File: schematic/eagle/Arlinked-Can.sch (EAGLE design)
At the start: 18 parts, among them U1 MCP2515, U2 TJA1050, U3 V_REG_LDOSMD, Y1 xtal

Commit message: Added schematic/protel/arlinked-can-v0.1-print-10p.pcb
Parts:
- added J8: JUMPER-1X3, Arlinked:JUMPER-1X3
- added R3: 10k, SparkFun:RESISTOR0603-RES
- added U$1: PAD, Arlinked:PAD
- C1, C3: value (none) -> 10uF
- C2: value (none) -> 407
- JP1: value (none) -> HOLE1
- JP2: value (none) -> HOLE2
- JP3: value (none) -> INPUT_HEADER
- LED1: value (none) -> 2mA
- R2: value (none) -> 320R
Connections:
- removed net N$7: F1.1, U3.OUT
- new net N$10: J8.J-2, R3.1
- new net S: J8.J-0, U2.S
- new net VCC-DIRECT: F1.1, JP7.J-2, U3.OUT
- net GND: now also J8.J-1; no longer U2.S
- net VCC: now also R3.2; no longer JP7.J-2
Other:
- moved on the sheet: C1, C2, F1, JP1, JP2, LED1, R1, R2, U1, U2, Y1

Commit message: Added Arlinked CanBus module v0.2
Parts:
- added C4, C5: (no value), SparkFun:CAP0402-CAP
- added LED2: 2mA Red, SparkFun:LED0603
- added R4: 320R, SparkFun:RESISTOR0402-RES
- added Y2: (no value), Arlinked:CRYSTALPAD-ONLY
- R1: device SparkFun:RESISTOR1206 -> SparkFun:RESISTOR0603-RES
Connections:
- net N$6 renamed LED1-CAN-2
- net VCC-DIRECT renamed VCC-FUSE
- removed net N$3: U1.OSC2, Y1.1
- removed net N$4: U1.OSC1, Y1.3
- new net LED2-POWER-2: LED2.A, R4.1
- new net OSC1: C4.1, U1.OSC1, Y1.3, Y2.2
- new net OSC2: C5.2, U1.OSC2, Y1.1, Y2.1
- net GND: now also C4.2, C5.1, LED2.C
- net VCC: now also R4.2
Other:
- moved on the sheet: LED1, R2, Y1
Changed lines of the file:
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@@
 <part name="GND4" library="SparkFun" deviceset="GND" device=""/>
 <part name="GND5" library="SparkFun" deviceset="GND" device=""/>
-<part name="R1" library="SparkFun" deviceset="RESISTOR" device="1206" value="10k"/>
+<part name="R1" library="SparkFun" deviceset="RESISTOR" device="0603-RES" value="10k"/>
 <part name="P+4" library="SparkFun" deviceset="VCC" device=""/>
 <part name="U1" library="Arlinked" deviceset="MCP2515" device=""/>
@@
 <part name="R3" library="SparkFun" deviceset="RESISTOR" device="0603-RES" value="10k"/>
 <part name="U$1" library="Arlinked" deviceset="PAD" device=""/>
+<part name="C4" library="SparkFun" deviceset="CAP" device="0402-CAP"/>
+<part name="C5" library="SparkFun" deviceset="CAP" device="0402-CAP"/>
+<part name="GND8" library="SparkFun" deviceset="GND" device=""/>
+<part name="Y2" library="Arlinked" deviceset="CRYSTAL" device="PAD-ONLY"/>
+<part name="LED2" library="SparkFun" deviceset="LED" device="0603" value="2mA Red"/>
+<part name="R4" library="SparkFun" deviceset="RESISTOR" device="0402-RES" value="320R"/>
+<part name="GND9" library="SparkFun" deviceset="GND" device=""/>
+<part name="P+5" library="SparkFun" deviceset="VCC" device=""/>
 </parts>
 <sheets>
@@
 <instance part="C2" gate="G$1" x="50.8" y="45.72"/>
 <instance part="GND1" gate="1" x="43.18" y="40.64"/>
-<instance part="Y1" gate="G$1" x="111.76" y="7.62"/>
-<instance part="GND2" gate="1" x="111.76" y="-2.54"/>
+<instance part="Y1" gate="G$1" x="111.76" y="12.7"/>
+<instance part="GND2" gate="1" x="111.76" y="2.54"/>
 <instance part="GND3" gate="1" x="88.9" y="2.54"/>
 <instance part="P+3" gate="1" x="55.88" y="71.12"/>
@@
 <instance part="C3" gate="G$1" x="-12.7" y="40.64"/>
 <instance part="F1" gate="G$1" x="30.48" y="50.8"/>
-<instance part="P+1" gate="1" x="50.8" y="50.8"/>
-<instance part="LED1" gate="G$1" x="124.46" y="5.08"/>
-<instance part="R2" gate="G$1" x="124.46" y="12.7" rot="R90"/>
-<instance part="GND7" gate="1" x="124.46" y="-2.54"/>
+<instance part="P+1" gate="1" x="43.18" y="50.8"/>
+<instance part="LED1" gate="G$1" x="124.46" y="30.48"/>
+<instance part="R2" gate="G$1" x="124.46" y="38.1" rot="R90"/>
+<instance part="GND7" gate="1" x="124.46" y="22.86"/>
 <instance part="U$2" gate="G$1" x="5.08" y="15.24" rot="MR180"/>
 <instance part="U2" gate="G$1" x="76.2" y="68.58"/>
@@
 <instance part="R3" gate="G$1" x="104.14" y="58.42" rot="R180"/>
 <instance part="U$1" gate="G$1" x="25.4" y="-22.86"/>
+<instance part="C4" gate="G$1" x="129.54" y="5.08"/>
+<instance part="C5" gate="G$1" x="124.46" y="7.62" rot="R180"/>
+<instance part="GND8" gate="1" x="124.46" y="0"/>
+<instance part="Y2" gate="G$1" x="127" y="10.16"/>
+<instance part="LED2" gate="G$1" x="-33.02" y="40.64"/>
+<instance part="R4" gate="G$1" x="-33.02" y="48.26" rot="R90"/>
+<instance part="GND9" gate="1" x="-33.02" y="33.02"/>
+<instance part="P+5" gate="1" x="-33.02" y="53.34"/>
 </instances>
 <busses>
@@
 <junction x="50.8" y="50.8"/>
 <junction x="43.18" y="50.8"/>
+</segment>
+<segment>
+<pinref part="R4" gate="G$1" pin="2"/>
+<pinref part="P+5" gate="1" pin="VCC"/>
 </segment>
 </net>
@@
 <pinref part="GND5" gate="1" pin="GND"/>
 </segment>
+<segment>
+<pinref part="C4" gate="G$1" pin="2"/>
+<pinref part="GND8" gate="1" pin="GND"/>
+<wire x1="129.54" y1="2.54" x2="124.46" y2="2.54" width="0.1524" layer="91"/>
+<pinref part="C5" gate="G$1" pin="1"/>
+<junction x="124.46" y="2.54"/>
+</segment>
+<segment>
+<pinref part="LED2" gate="G$1" pin="C"/>
+<pinref part="GND9" gate="1" pin="GND"/>
+</segment>
 </net>
 <net name="N$1" class="0">
@@
 </segment>
 </net>
-<net name="N$3" class="0">
+<net name="OSC2" class="0">
+<segment>
+<wire x1="119.38" y1="15.24" x2="124.46" y2="15.24" width="0.1524" layer="91"/>
+<wire x1="124.46" y1="15.24" x2="124.46" y2="10.16" width="0.1524" layer="91"/>
+<pinref part="C5" gate="G$1" pin="2"/>
+<pinref part="Y2" gate="G$1" pin="1"/>
+<label x="119.38" y="15.24" size="1.778" layer="95"/>
+<junction x="124.46" y="10.16"/>
+</segment>
 <segment>
 <pinref part="Y1" gate="G$1" pin="1"/>
+<wire x1="109.22" y1="15.24" x2="109.22" y2="12.7" width="0.1524" layer="91"/>
 <wire x1="106.68" y1="15.24" x2="109.22" y2="15.24" width="0.1524" layer="91"/>
-<wire x1="109.22" y1="15.24" x2="109.22" y2="7.62" width="0.1524" layer="91"/>
 <pinref part="U1" gate="G$1" pin="OSC2"/>
-</segment>
-</net>
-<net name="N$4" class="0">
+<junction x="109.22" y="12.7"/>
+</segment>
+</net>
+<net name="OSC1" class="0">
+<segment>
+<wire x1="119.38" y1="17.78" x2="129.54" y2="17.78" width="0.1524" layer="91"/>
+<wire x1="129.54" y1="17.78" x2="129.54" y2="10.16" width="0.1524" layer="91"/>
+<pinref part="C4" gate="G$1" pin="1"/>
+<pinref part="Y2" gate="G$1" pin="2"/>
+<label x="119.38" y="17.78" size="1.778" layer="95"/>
+<junction x="129.54" y="10.16"/>
+</segment>
 <segment>
 <pinref part="Y1" gate="G$1" pin="3"/>
+<wire x1="114.3" y1="17.78" x2="114.3" y2="12.7" width="0.1524" layer="91"/>
 <wire x1="106.68" y1="17.78" x2="114.3" y2="17.78" width="0.1524" layer="91"/>
-<wire x1="114.3" y1="17.78" x2="114.3" y2="7.62" width="0.1524" layer="91"/>
 <pinref part="U1" gate="G$1" pin="OSC1"/>
+<junction x="114.3" y="12.7"/>
 </segment>
 </net>
@@
 <segment>
 <pinref part="U1" gate="G$1" pin="SCK"/>
-<wire x1="106.68" y1="27.94" x2="124.46" y2="27.94" width="0.1524" layer="91"/>
+<wire x1="106.68" y1="27.94" x2="119.38" y2="27.94" width="0.1524" layer="91"/>
 <label x="109.22" y="27.94" size="1.778" layer="95"/>
-<pinref part="R2" gate="G$1" pin="2"/>
-<wire x1="124.46" y1="27.94" x2="124.46" y2="17.78" width="0.1524" layer="91"/>
 </segment>
 <segment>
@@
 <wire x1="55.88" y1="7.62" x2="45.72" y2="7.62" width="0.1524" layer="91"/>
 <label x="45.72" y="7.62" size="1.778" layer="95"/>
+</segment>
+<segment>
+<pinref part="R2" gate="G$1" pin="2"/>
+<wire x1="124.46" y1="43.18" x2="121.92" y2="43.18" width="0.1524" layer="91"/>
+<label x="119.38" y="43.18" size="1.778" layer="95"/>
 </segment>
 </net>
@@
 </segment>
 </net>
-<net name="N$6" class="0">
+<net name="LED1-CAN-2" class="0">
 <segment>
 <pinref part="R2" gate="G$1" pin="1"/>
@@
 </segment>
 </net>
-<net name="VCC-DIRECT" class="0">
+<net name="VCC-FUSE" class="0">
 <segment>
 <pinref part="U3" gate="G$1" pin="OUT"/>
@@
 <wire x1="20.32" y1="50.8" x2="20.32" y2="55.88" width="0.1524" layer="91"/>
 <label x="17.78" y="55.88" size="1.778" layer="95"/>
+<junction x="20.32" y="50.8"/>
 </segment>
 <segment>
@@
 </segment>
 </net>
+<net name="LED2-POWER-2" class="0">
+<segment>
+<pinref part="R4" gate="G$1" pin="1"/>
+<pinref part="LED2" gate="G$1" pin="A"/>
+</segment>
+</net>

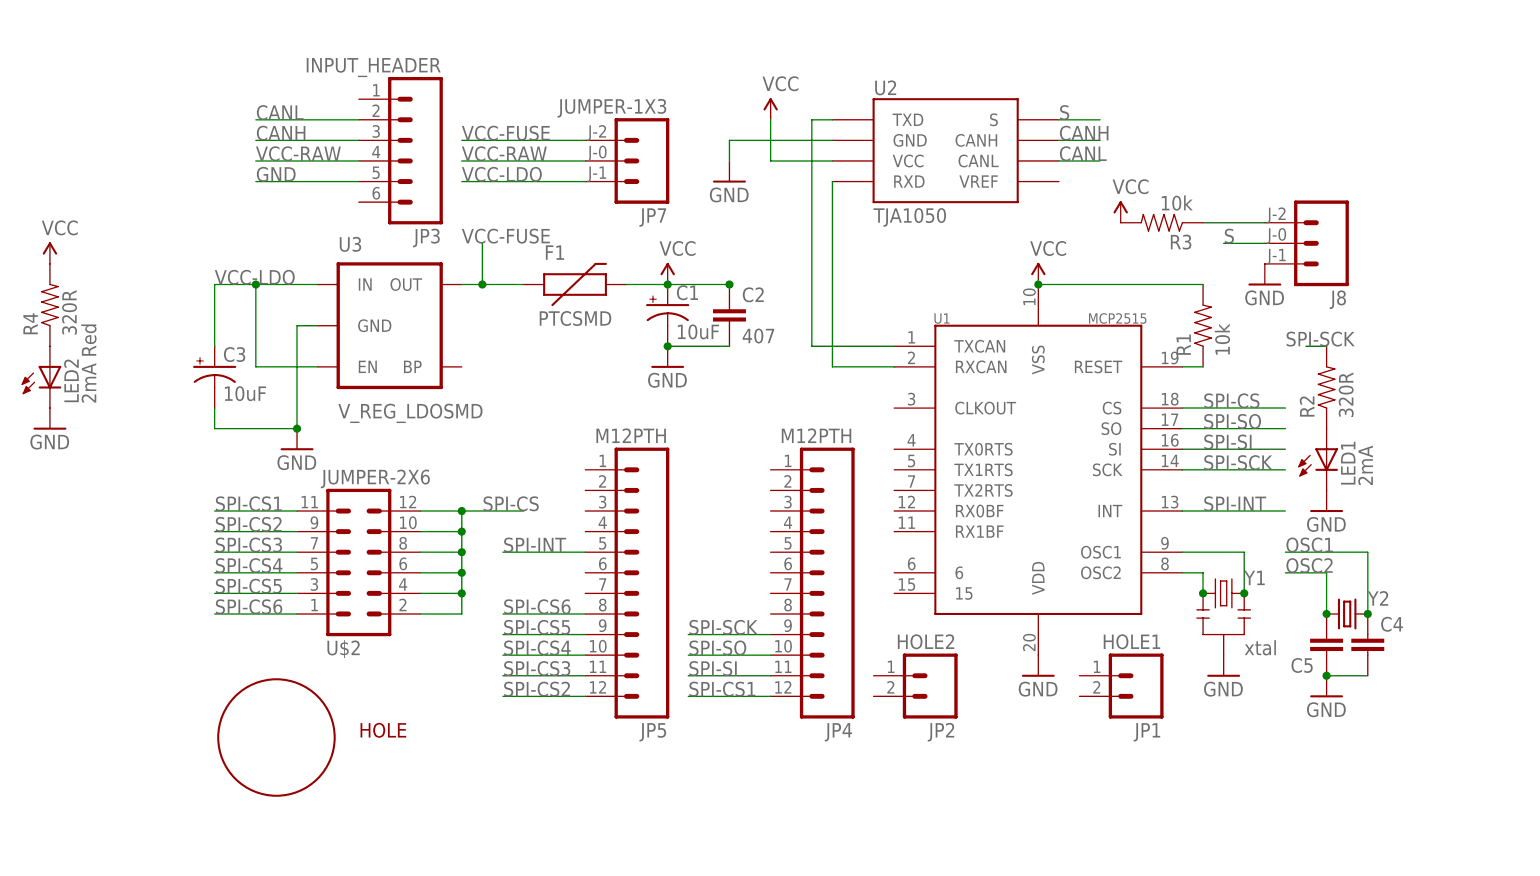
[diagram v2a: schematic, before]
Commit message: CanBus module v0.2 schematic and PCB release  #4 fixed Vdd Vss mistake
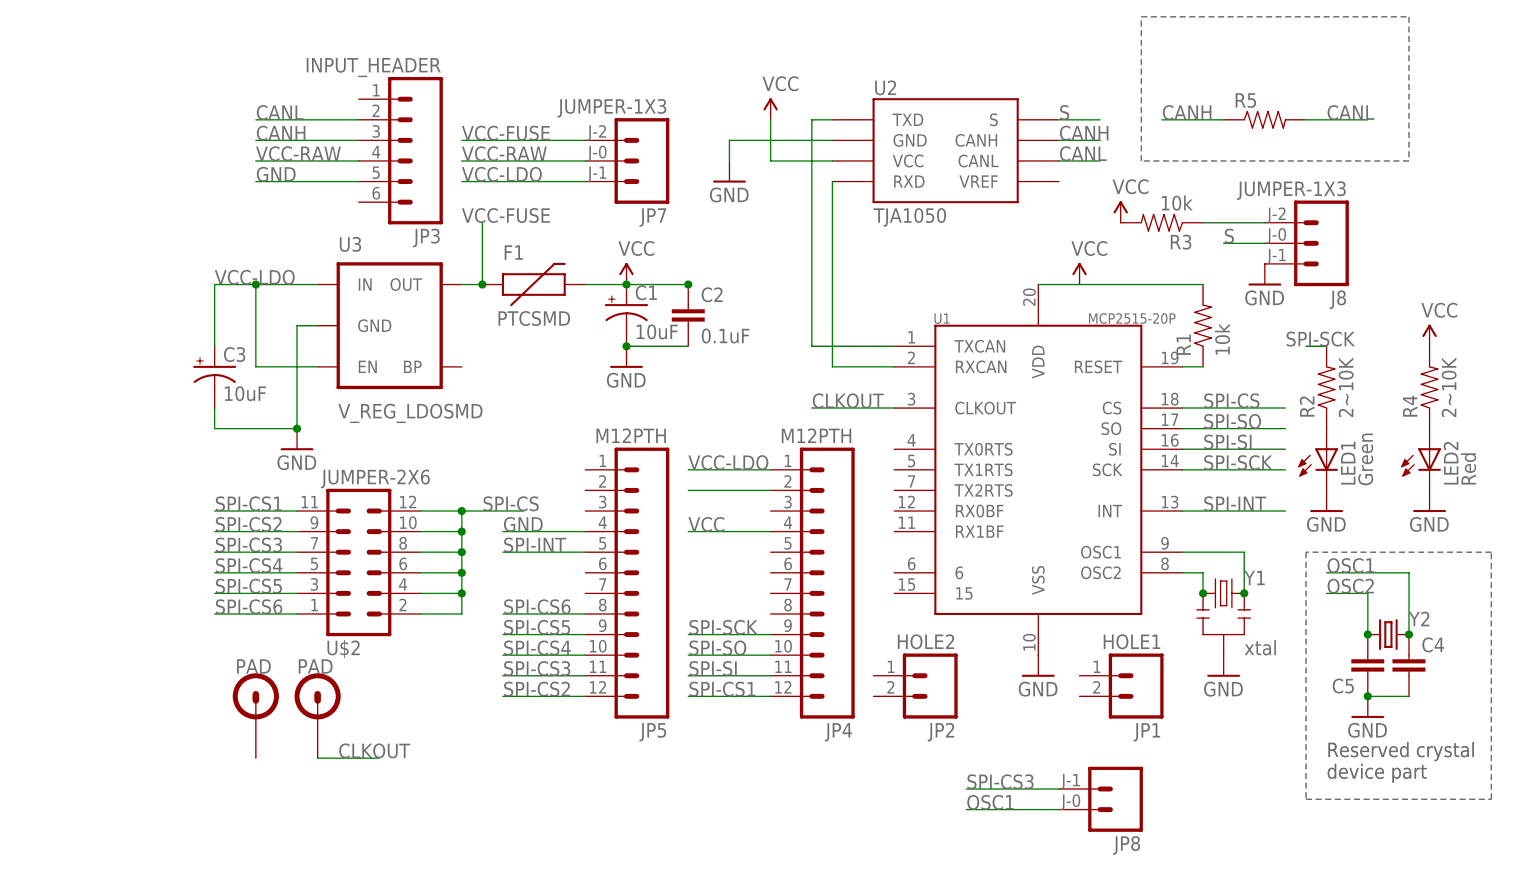
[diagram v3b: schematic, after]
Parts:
- added JP8: JUMPER-1X2, Arlinked:JUMPER-1X2
- added R5: (no value), SparkFun:RESISTOR0603-RES
- added U$3: PAD_SMD, Arlinked:PAD_SMD
- C2: value 407 -> 0.1uF
- LED1: value 2mA -> Green
- LED2: value 2mA Red -> Red
- R2: value 320R -> 2~10K; device SparkFun:RESISTOR0603-RES -> SparkFun:RESISTOR0402-RES
- R4: value 320R -> 2~10K
- U1: value MCP2515 -> MCP2515-20P; device Arlinked:MCP2515 -> Arlinked:MCP2515-20P
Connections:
- new net CLKOUT: U$3.P$1, U1.CLKOUT
- net CANH: now also R5.1
- net CANL: now also R5.2
- net GND: now also JP4.2, JP5.4, U1.VSS; no longer U1.VDD
- net OSC1: now also JP8.J-1
- net SPI-CS3: now also JP8.J-0
- net VCC: now also JP4.4, U1.VDD; no longer U1.VSS
- net VCC-LDO: now also JP4.1
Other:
- note added: "Reserved crystal device part"
- moved on the sheet: C1, C2, C4, C5, F1, LED2, R4, Y2
